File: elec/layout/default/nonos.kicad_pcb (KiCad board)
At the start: 2 copper layers, 45 x 122 mm, 74 parts, among them CN1 HRSHirose_DF40C_100DS_0_4V51, CN2 HRSHirose_DF40C_100DS_0_4V51, Q1 MOSFET, U1 STUSB4500QTR, U2 _Texas_Instruments_SN74LVC1G0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, U3 _Texas_Instruments_TAS5825MRH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, U5 JST_Sales_America_B02B_XASK_1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, U6 JST_Sales_America_B02B_XASK_1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, U7 _Texas_Instruments_TPS56637RP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

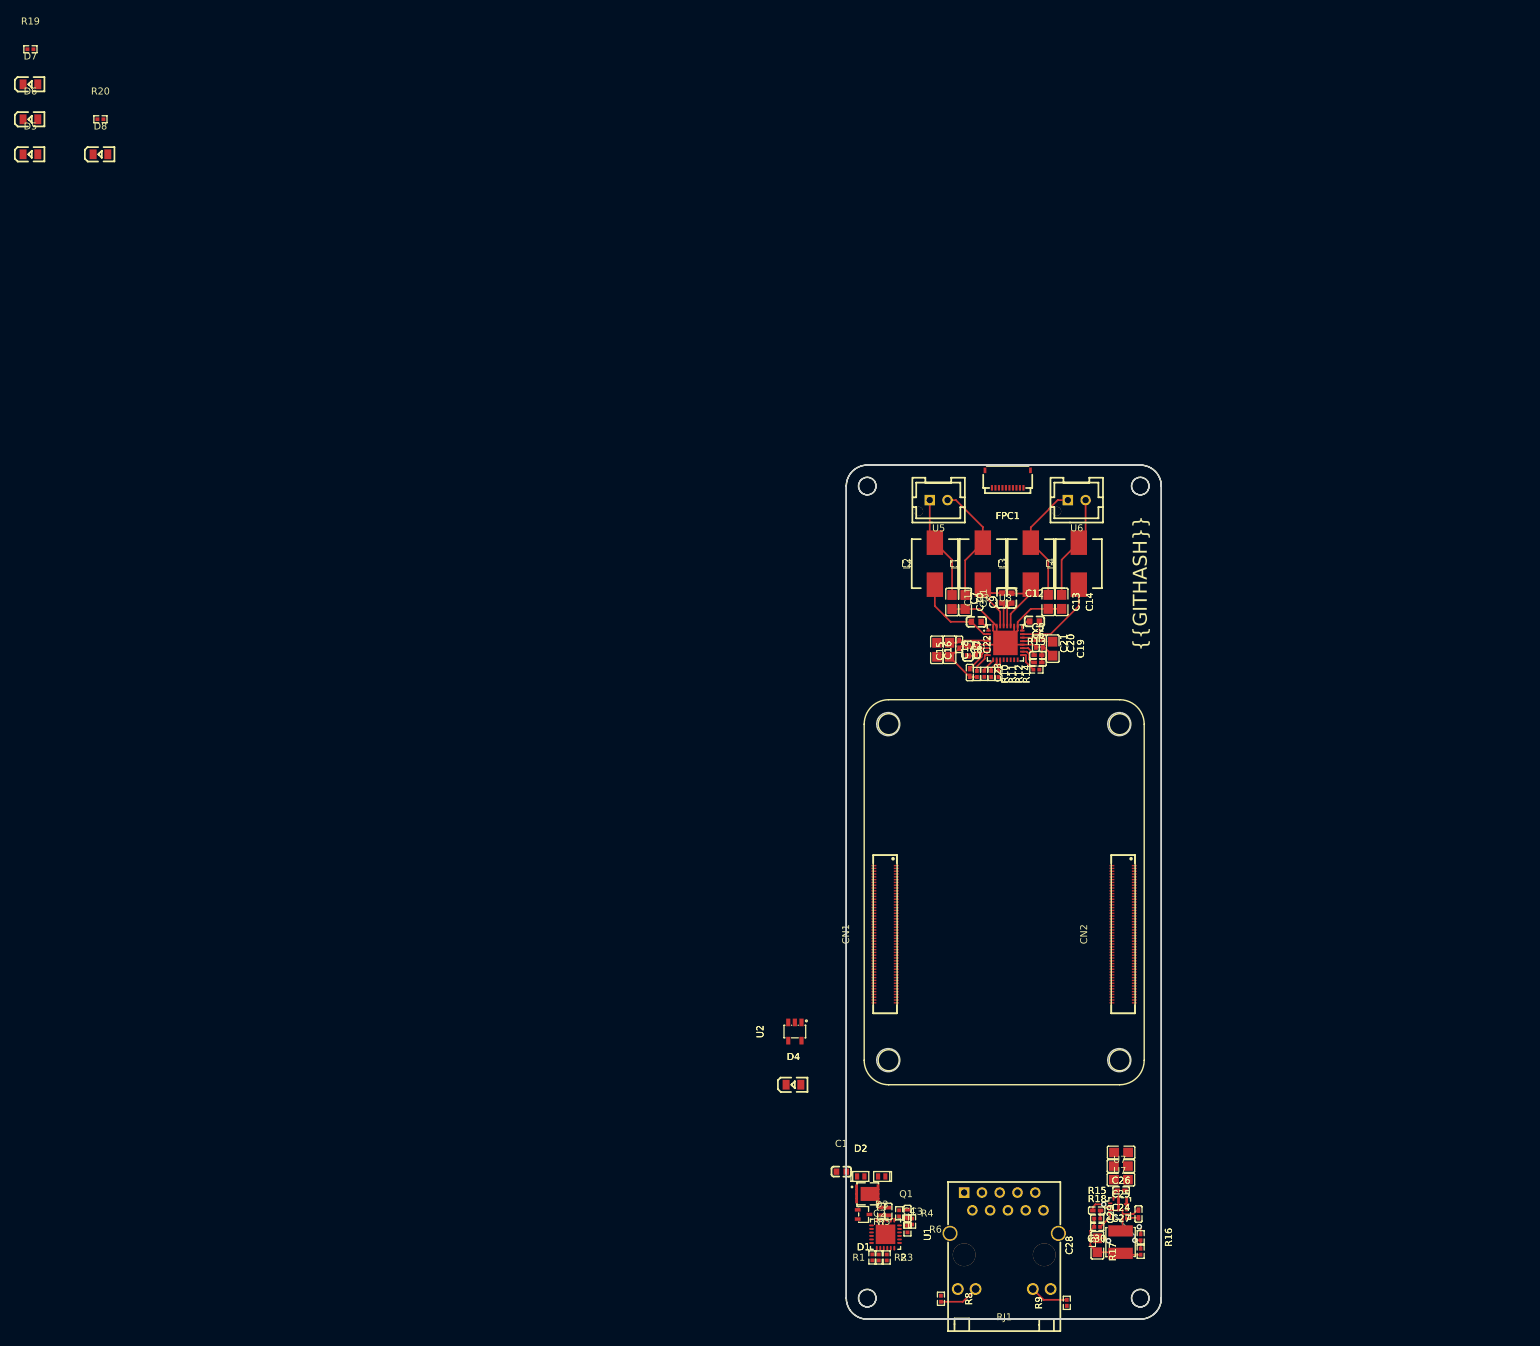
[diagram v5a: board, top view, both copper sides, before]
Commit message: refactor PD controller + remove params
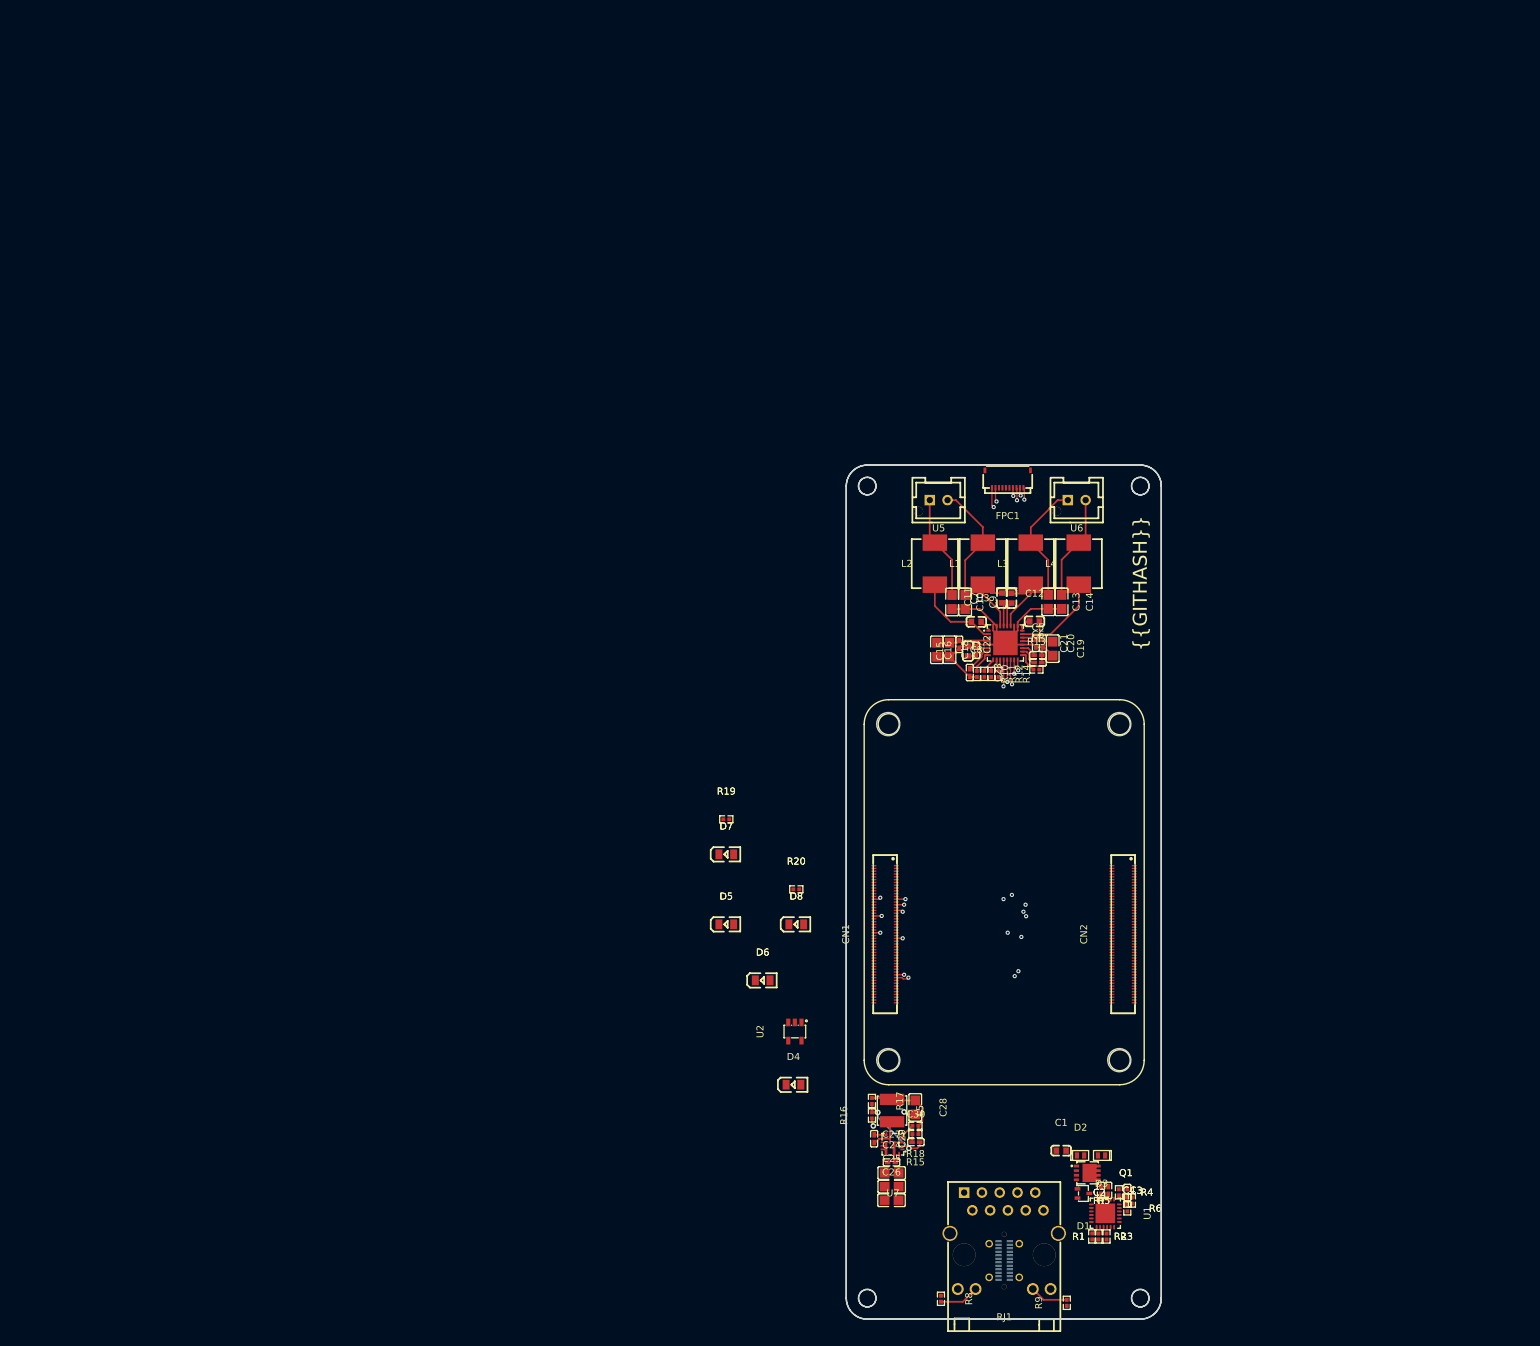
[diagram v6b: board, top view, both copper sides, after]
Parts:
- added U4: _HCTL_HC_TYPE_C_24P_VS9_3_5A_F1_1_04, lcsc:USB-C-SMD_HC-TYPE-C-24P-VS9.3-5A-F1.1-04, B.Cu at (139.1, 158.0)
- moved D6 161.5 mm to (104.6, 118.0)
- moved D5 148.3 mm to (99.4, 110.0)
- moved D7 148.3 mm to (99.4, 100.0)
- moved D8 148.3 mm to (109.4, 110.0)
- moved R19 148.3 mm to (99.4, 95.0)
- moved R20 148.3 mm to (109.4, 105.0)
- moved R17 44.0 mm to (120.2, 135.2), turned to -90 degrees
- moved R16 42.1 mm to (120.2, 137.3), turned to 90 degrees
- moved C29 39.3 mm to (120.5, 140.6), turned to -90 degrees
- moved L5 37.7 mm to (123.1, 136.6), turned to -90 degrees
- moved U7 33.7 mm to (123.2, 141.4), turned to 180 degrees
- moved C26 33.5 mm to (123.0, 149.4), turned to 0 degrees
- moved C27 33.0 mm to (123.0, 144.0), turned to 0 degrees
- moved C25 32.9 mm to (123.0, 147.5), turned to 0 degrees
- moved C24 32.8 mm to (123.0, 145.5), turned to 0 degrees
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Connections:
- net cathode renamed processor.power_3v3_led-cathode
- net cathode-1 renamed processor.power_5v_led-cathode
- net cathode-2 renamed processor.power_1v8_led-cathode
- C1 pad 1: lv -> GND
- C10 pad 2: lv -> GND
- C11 pad 1: amplifier-net-11 -> amplifier-net-5
- C11 pad 2: amplifier-net-2 -> amplifier-net-4
- C12 pad 1: amplifier-net-5 -> amplifier-net-3
- C12 pad 2: amplifier-net-6 -> amplifier-net-1
- C13 pad 1: net-4 -> net-3
- C13 pad 2: lv -> GND
- C14 pad 2: lv -> GND
- C15 pad 2: lv -> GND
- C16 pad 2: lv -> GND
- C17 pad 2: lv -> GND
- C18 pad 2: lv -> GND
- C19 pad 2: lv -> GND
- C2 pad 1: pd_controller-net-1 -> pd_controller-net-4
- C20 pad 2: lv -> GND
- C21 pad 2: lv -> GND
- C22 pad 2: lv -> GND
- C23 pad 1: amplifier-net-4 -> amplifier-net-7
- C23 pad 2: lv -> GND
- C24 pad 2: lv -> GND
- C25 pad 2: lv -> GND
- C26 pad 2: lv -> GND
- C27 pad 2: lv -> GND
- C28 pad 1: net-3 -> VCC_5V
- C28 pad 2: lv -> GND
- C29 pad 1: regulator-net-3 -> regulator-net-4
- C29 pad 2: regulator-net-2 -> regulator-net-3
- C3 pad 1: lv -> GND
- C4 pad 1: lv -> GND
- C5 pad 1: amplifier-net-8 -> amplifier-net-10
- C5 pad 2: lv -> GND
- C6 pad 1: amplifier-net-7 -> amplifier-net
- C6 pad 2: lv -> GND
- C7 pad 1: amplifier-net-10 -> amplifier-net-6
- C8 pad 1: amplifier-net-1 -> amplifier-net-2
- C8 pad 2: amplifier-net -> amplifier-net-8
- C9 pad 2: lv -> GND
- CN1 pad 10: pins[19] -> processor-net-3
- CN1 pad 14: processor-signal-7 -> processor-signal-3
- CN1 pad 15: signal-1 -> signal-7
- CN1 pad 17: signal-2 -> signal-5
- CN1 pad 23: processor-signal-2 -> processor-signal-6
- CN1 pad 24: processor-signal-5 -> processor-signal-7
- CN1 pad 28: signal -> signal-3
- CN1 pad 29: signal-7 -> signal-2
- CN1 pad 73: processor-signal-3 -> processor-signal-5
- CN1 pad 75: processor-signal-4 -> processor-signal-2
- CN1 pad 77: processor-signal-6 -> processor-signal-1
- CN1 pad 78: processor-pins[44] -> processor-pins[44]-1
- CN1 pad 81: processor-signal-1 -> processor-signal-9
- CN1 pad 82: signal-3 -> signal-6
- CN1 pad 85: processor-signal-9 -> processor-signal-4
- CN2 pad 78: processor-pins[44]-1 -> processor-pins[44]
- D1 pad 3: lv -> GND
- D2 pad 2: lv -> GND
- D3 pad 2: lv -> GND
- D4 pad 1: processor-net-2 -> VCC_3V3
- D5 pad 1: VCC_1V8 -> processor.power_1v8_led-anode
- D6 pad 1: VCC_3V3 -> processor.power_3v3_led-anode
- D7 pad 1: VCC_5V -> processor.power_5v_led-anode
- D8 pad 2: processor-net-1 -> processor-net-2
- FPC1 pad 10: signal-3 -> signal-6
- FPC1 pad 3: lv -> GND
- FPC1 pad 4: net-3 -> VCC_5V
- FPC1 pad 6: lv -> GND
- FPC1 pad 8: signal-2 -> signal-5
- FPC1 pad 9: signal-1 -> signal-7
- L2 pad 1: amplifier-net -> amplifier-net-8
- L3 pad 1: amplifier-net-2 -> amplifier-net-4
- L3 pad 2: net-4 -> net-3
- L4 pad 1: amplifier-net-6 -> amplifier-net-1
- L5 pad 1: net-3 -> VCC_5V
- L5 pad 2: regulator-net-2 -> regulator-net-3
- R10 pad 1: amplifier-net-3 -> amplifier-net-11
- R10 pad 2: lv -> GND
- R11 pad 1: signal-7 -> signal-2
- R12 pad 1: signal-5 -> signal
- R13 pad 1: signal -> signal-3
- R14 pad 1: signal-6 -> signal-1
- R15 pad 1: net-3 -> VCC_5V
- R16 pad 1: lv -> GND
- R17 pad 1: net-3 -> VCC_5V
- R18 pad 1: net-3 -> VCC_5V
- R18 pad 2: regulator-net-4 -> regulator-net-2
- R19 pad 2: VCC_3V3 -> processor-net-1
- R20 pad 1: processor-net-1 -> processor-net-2
- R20 pad 2: GND -> processor-net-3
- R6 pad 2: pd_controller-net-4 -> pd_controller-net-1
- R7 pad 2: pd_controller-net-1 -> pd_controller-net-4
- R8 pad 2: rj45-net -> rj45-net-1
- R9 pad 2: rj45-net-1 -> rj45-net
- RJ1 pad 12: rj45-net -> rj45-net-1
- RJ1 pad 13: rj45-net-1 -> rj45-net
- RJ1 pad SHIELD0: lv -> GND
- RJ1 pad SHIELD1: lv -> GND
- U1 pad 10: lv -> GND
- U1 pad 12: lv -> GND
- U1 pad 13: lv -> GND
- U1 pad 16: pd_controller-net-4 -> pd_controller-net-1
- U1 pad 22: lv -> GND
- U1 pad 25: lv -> GND
- U1 pad 6: lv -> GND
- U2 pad 4: processor-net-2 -> processor-net-1
- U3 pad 1: amplifier-net-1 -> amplifier-net-2
- U3 pad 10: signal-5 -> signal
- U3 pad 11: signal-6 -> signal-1
- U3 pad 17: signal -> signal-3
- U3 pad 18: amplifier-net-7 -> amplifier-net
- U3 pad 19: amplifier-net-8 -> amplifier-net-10
- U3 pad 2: amplifier-net -> amplifier-net-8
- U3 pad 20: lv -> GND
- U3 pad 23: amplifier-net-6 -> amplifier-net-1
- U3 pad 24: amplifier-net-5 -> amplifier-net-3
- U3 pad 25: lv -> GND
- U3 pad 26: lv -> GND
- U3 pad 27: amplifier-net-2 -> amplifier-net-4
- U3 pad 28: amplifier-net-11 -> amplifier-net-5
- U3 pad 29: amplifier-net-10 -> amplifier-net-6
- U3 pad 31: lv -> GND
- U3 pad 32: lv -> GND
- U3 pad 33: lv -> GND
- U3 pad 5: lv -> GND
- U3 pad 7: amplifier-net-4 -> amplifier-net-7
- U3 pad 8: amplifier-net-3 -> amplifier-net-11
- U3 pad 9: signal-7 -> signal-2
- U6 pad 1: net-4 -> net-3
- U7 pad 10: lv -> GND
- U7 pad 3: lv -> GND
- U7 pad 4: regulator-net-4 -> regulator-net-2
- U7 pad 6: regulator-net-2 -> regulator-net-3
- U7 pad 7: regulator-net-3 -> regulator-net-4
- U7 pad 9: lv -> GND
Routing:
- net SDA: track 0.00 -> 91.0 mm, vias 0 -> 4
- net SCL: track 0.00 -> 90.2 mm, vias 0 -> 4
- net signal-4: track 0.00 -> 84.9 mm, vias 0 -> 3
- net signal-6: track 3.34 -> 87.3 mm, vias 0 -> 3
- net signal-5: track 1.70 -> 82.1 mm, vias 0 -> 3
- net signal-7: track 2.11 -> 81.6 mm, vias 0 -> 3
- net GND: track 0.00 -> 59.2 mm, vias 0 -> 2
- net lv: track 59.2 -> 0.00 mm, vias 2 -> 0
- net I2S_SCK: track 0.00 -> 58.1 mm, vias 0 -> 3
- net I2S_SD: track 0.00 -> 54.0 mm, vias 0 -> 3
- net I2S_WS: track 0.00 -> 49.8 mm, vias 0 -> 3
- net net-4: track 17.4 -> 0.00 mm
- net VCC_5V: track 0.00 -> 11.8 mm
- net amplifier-net-5: track 14.6 -> 3.53 mm
- net regulator-net: track 1.80 -> 12.3 mm, vias 0 -> 2
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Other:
- copper layers 2 -> 4

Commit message: layout 95%
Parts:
- removed D6, D7, D8: , lcsc:LED0805-R-RD
- added HDR1: HCTL_PZ254_2_04_S, lcsc:HDR-SMD_8P-P2.54-V-M-R2-C4-LS7.4, F.Cu at (169.4, 130.9)
- added HDR2: HCTL_PZ254_2_04_S, lcsc:HDR-SMD_8P-P2.54-V-M-R2-C4-LS7.4, F.Cu at (169.4, 62.9)
- C2: value 100nF ±10% 16V X7R -> 1µF ±10% 25V X5R
- C4: value 1µF ±10% 25V X5R -> 100nF ±10% 16V X7R
- moved D4 76.2 mm to (134.6, 61.1), turned to 90 degrees
- moved U2 63.2 mm to (133.0, 66.7), turned to -90 degrees
- moved D5 59.1 mm to (132.6, 61.1), turned to 90 degrees
- moved R20 47.3 mm to (133.3, 64.1)
- moved R19 46.9 mm to (135.0, 64.5), turned to -90 degrees
- moved R3 22.5 mm to (137.3, 138.0), turned to 90 degrees
- moved R1 21.6 mm to (137.7, 140.1), turned to 0 degrees
- moved R2 21.3 mm to (138.3, 138.0), turned to 90 degrees
- moved R6 21.1 mm to (137.3, 142.3), turned to 0 degrees
- moved R5 21.0 mm to (137.3, 143.3), turned to 180 degrees
- moved R7 18.6 mm to (139.1, 143.5), turned to 0 degrees
- moved D3 17.8 mm to (135.2, 143.0), turned to 0 degrees
- moved U4 16.8 mm to (153.2, 149.0)
- moved C23 16.6 mm to (148.4, 65.4)
- moved R11 16.6 mm to (150.5, 65.6)
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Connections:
- net pd_controller.PD_CONTROLLER-signal renamed pd_controller.pd_controller-signal-1
- net pd_controller.PD_CONTROLLER-signal-1 renamed pd_controller.pd_controller-signal
- net pd_controller.PD_CONTROLLER.footprint.pins[18].net-net renamed pd_controller.pd_controller.footprint.pins[18].net-net
- net pins[40] renamed processor.hdi_b-pins[40]
- net pins[46] renamed processor-pins[46]-1
- net pins[49] renamed processor.hdi_b-pins[49]
- net processor-signal-8 renamed processor-pins[49]
- net processor.hdi_b-pins[23] renamed pins[23]
- net processor.hdi_b-pins[26] renamed pins[26]
- net processor.hdi_b-pins[28] renamed pins[28]
- C10 pad 1: net -> net-2
- C11 pad 1: amplifier-net-5 -> amplifier-net-3
- C11 pad 2: amplifier-net-4 -> amplifier-net-2
- C12 pad 1: amplifier-net-3 -> amplifier-net-7
- C12 pad 2: amplifier-net-1 -> amplifier-net
- C13 pad 1: net-3 -> net-1
- C14 pad 1: net-1 -> net
- C2 pad 1: pd_controller-net-4 -> GND
- C2 pad 2: VBUS -> VREG_1V2
- C23 pad 1: amplifier-net-7 -> amplifier-net-6
- C29 pad 1: regulator-net-4 -> regulator-net
- C29 pad 2: regulator-net-3 -> regulator-net-1
- C3 pad 2: VREG_1V2 -> VREG_2V7
- C30 pad 1: regulator-net-1 -> regulator-net-2
- C30 pad 2: regulator-net -> regulator-net-3
- C4 pad 1: GND -> pd_controller-net-3
- C4 pad 2: VREG_2V7 -> VBUS
- C6 pad 1: amplifier-net -> amplifier-net-1
- C7 pad 1: amplifier-net-6 -> amplifier-net-11
- C7 pad 2: amplifier-net-9 -> amplifier-net-8
- C8 pad 1: amplifier-net-2 -> amplifier-net-4
- C8 pad 2: amplifier-net-8 -> amplifier-net-5
- C9 pad 1: net-2 -> net-3
- CN1 pad 10: processor-net-3 -> processor-net-2
- CN1 pad 12: processor-pins[23] -> processor-signal
- CN1 pad 14: processor-signal-3 -> UART_TX
- CN1 pad 15: signal-7 -> signal-3
- CN1 pad 17: signal-5 -> signal-4
- CN1 pad 22: pins[43] -> processor-signal-3
- CN1 pad 23: processor-signal-6 -> pins[45]
- CN1 pad 24: processor-signal-7 -> processor-signal-2
- CN1 pad 27: signal-4 -> signal-5
- CN1 pad 28: signal-3 -> signal-2
- CN1 pad 29: signal-2 -> signal-1
- CN1 pad 73: processor-signal-5 -> UART_RX
- CN1 pad 75: processor-signal-2 -> pins[50]
- CN1 pad 77: processor-signal-1 -> processor-pins[46]
- CN1 pad 78: processor-pins[44]-1 -> processor-pins[44]
- CN1 pad 80: processor-signal -> processor-pins[40]
- CN1 pad 81: processor-signal-9 -> processor-signal-1
- CN1 pad 82: signal-6 -> signal
- CN1 pad 85: processor-signal-4 -> processor-signal-6
- CN1 pad 86: processor-pins[28] -> processor-signal-5
- CN1 pad 87: processor-pins[26] -> processor-signal-4
- CN2 pad 78: processor-pins[44] -> processor-pins[44]-1
- D4 pad 2: processor-net -> processor-net-3
- D5 pad 1: processor.power_1v8_led-anode -> VCC_3V3
- D5 pad 2: processor.power_1v8_led-cathode -> processor-net-1
- FPC1 pad 10: signal-6 -> signal
- FPC1 pad 7: signal-4 -> signal-5
- FPC1 pad 8: signal-5 -> signal-4
- FPC1 pad 9: signal-7 -> signal-3
- L1 pad 1: amplifier-net-9 -> amplifier-net-8
- L1 pad 2: net-2 -> net-3
- L2 pad 1: amplifier-net-8 -> amplifier-net-5
- L2 pad 2: net -> net-2
- L3 pad 1: amplifier-net-4 -> amplifier-net-2
- L3 pad 2: net-3 -> net-1
- L4 pad 1: amplifier-net-1 -> amplifier-net
- L4 pad 2: net-1 -> net
- L5 pad 2: regulator-net-3 -> regulator-net-1
- Q1 pad 1: pd_controller.VSINK_MOSFET.footprint.pins[0].net-net -> VBUS
- Q1 pad 2: pd_controller.VSINK_MOSFET.footprint.pins[1].net-net -> VBUS
- Q1 pad 4: pd_controller-net -> pd_controller-net-2
- Q1 pad 5: pd_controller.VSINK_MOSFET.footprint.pins[4].net-net -> VSINK_VCC
- Q1 pad 6: pd_controller.VSINK_MOSFET.footprint.pins[5].net-net -> VSINK_VCC
- Q1 pad 7: pd_controller.VSINK_MOSFET.footprint.pins[6].net-net -> VSINK_VCC
- Q1 pad 8: pd_controller.VSINK_MOSFET.footprint.pins[7].net-net -> VSINK_VCC
- R1 pad 2: pd_controller-net-3 -> pd_controller-net-1
- R10 pad 1: amplifier-net-11 -> amplifier-net-9
- R11 pad 1: signal-2 -> signal-1
- R12 pad 1: signal -> signal-7
- R13 pad 1: signal-3 -> signal-2
- R14 pad 1: signal-1 -> signal-6
- R15 pad 2: regulator-net-1 -> regulator-net-2
- R16 pad 2: regulator-net -> regulator-net-3
- R17 pad 2: regulator-net -> regulator-net-3
- R18 pad 2: regulator-net-2 -> regulator-net-4
- R19 pad 1: processor-net -> processor-net-3
- R19 pad 2: processor-net-1 -> processor-net-2
- R2 pad 1: I2C_SCL -> SCL
- R2 pad 2: hv -> VCC_3V3
- R20 pad 1: processor-net-2 -> processor-net-1
- R20 pad 2: processor-net-3 -> processor-net
- R3 pad 1: I2C_SDA -> SDA
- R3 pad 2: hv -> VCC_3V3
- R4 pad 2: pd_controller-net-2 -> pd_controller-net
- R5 pad 1: pd_controller-net -> pd_controller-net-2
- R6 pad 1: pd_controller-net -> pd_controller-net-2
- R6 pad 2: pd_controller-net-1 -> pd_controller-net-4
- R7 pad 1: pd_controller-net -> pd_controller-net-2
- R7 pad 2: pd_controller-net-4 -> pd_controller-net-3
- U1 pad 16: pd_controller-net-1 -> pd_controller-net-4
- U1 pad 18: pd_controller-net-2 -> pd_controller-net
- U1 pad 7: I2C_SCL -> SCL
- U1 pad 8: I2C_SDA -> SDA
- U1 pad 9: pd_controller-net-3 -> pd_controller-net-1
- U2 pad 4: processor-net-1 -> processor-net
- U3 pad 1: amplifier-net-2 -> amplifier-net-4
- U3 pad 10: signal -> signal-7
- U3 pad 11: signal-1 -> signal-6
- U3 pad 17: signal-3 -> signal-2
- U3 pad 18: amplifier-net -> amplifier-net-1
- U3 pad 2: amplifier-net-8 -> amplifier-net-5
- U3 pad 23: amplifier-net-1 -> amplifier-net
- U3 pad 24: amplifier-net-3 -> amplifier-net-7
- U3 pad 27: amplifier-net-4 -> amplifier-net-2
- U3 pad 28: amplifier-net-5 -> amplifier-net-3
- U3 pad 29: amplifier-net-6 -> amplifier-net-11
- U3 pad 30: amplifier-net-9 -> amplifier-net-8
- U3 pad 7: amplifier-net-7 -> amplifier-net-6
- U3 pad 8: amplifier-net-11 -> amplifier-net-9
- U3 pad 9: signal-2 -> signal-1
- U4 pad 25: usb_connector.connector-net -> GND
- U4 pad 26: usb_connector.connector-net -> GND
- U4 pad 27: usb_connector.connector-net -> GND
- U4 pad 28: usb_connector.connector-net -> GND
- U4 pad A1: usb_connector.connector-net-1 -> GND
- U4 pad A12: usb_connector.connector-net-1 -> GND
- U4 pad A4: VSINK_VCC -> VBUS
- U4 pad A6: usb_connector-net-1 -> usb_connector-net
- U4 pad A7: usb_connector-net -> usb_connector-net-1
- U4 pad A9: VSINK_VCC -> VBUS
- U4 pad B1: usb_connector.connector-net-1 -> GND
- U4 pad B12: usb_connector.connector-net-1 -> GND
- U4 pad B4: VSINK_VCC -> VBUS
- U4 pad B5: CC1 -> CC2
- U4 pad B6: usb_connector-net-1 -> usb_connector-net
- U4 pad B7: usb_connector-net -> usb_connector-net-1
- U4 pad B9: VSINK_VCC -> VBUS
- U5 pad 1: net -> net-2
- U5 pad 2: net-2 -> net-3
- U6 pad 1: net-3 -> net-1
- U6 pad 2: net-1 -> net
- U7 pad 2: regulator-net -> regulator-net-3
- U7 pad 4: regulator-net-2 -> regulator-net-4
- U7 pad 6: regulator-net-3 -> regulator-net-1
- U7 pad 7: regulator-net-4 -> regulator-net
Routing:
- net VCC_5V: track 11.8 -> 136.2 mm, vias 0 -> 4
- net signal-6: track 87.3 -> 1.70 mm, vias 3 -> 0
- net signal: track 1.91 -> 87.2 mm, vias 0 -> 3
- net signal-7: track 81.6 -> 1.91 mm, vias 3 -> 0
- net signal-3: track 3.34 -> 82.1 mm, vias 0 -> 3
- net ETH_LED_ACTIVITY: track 0.00 -> 78.5 mm, vias 0 -> 2
- net ETH_LED_LINK: track 0.00 -> 70.0 mm, vias 0 -> 2
- net ETH_P3_N: track 0.00 -> 69.5 mm, vias 0 -> 2
- net ETH_P3_P: track 0.00 -> 68.8 mm, vias 0 -> 2
- net ETH_P1_P: track 0.00 -> 67.0 mm, vias 0 -> 1
- net SDA: track 91.0 -> 157.3 mm, vias 4 -> 6
- net SCL: track 90.2 -> 154.3 mm, vias 4 -> 6
- net ETH_P2_N: track 0.00 -> 63.5 mm, vias 0 -> 2
- net ETH_P2_P: track 0.00 -> 60.3 mm, vias 0 -> 2
- net ETH_P1_N: track 0.00 -> 58.1 mm, vias 0 -> 1
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- added copper zone on F.Cu, net GND
- added copper zone on In2.Cu, net GND
- added copper zone on F.Cu, net VBUS
- added copper zone on F.Cu, net VCC_5V
- added copper zone on B.Cu, net VSINK_VCC
- added copper zone on F.Cu, net VSINK_VCC
- added copper zone on F.Cu, net amplifier-net
- added copper zone on F.Cu, net amplifier-net-2
- added copper zone on F.Cu, net amplifier-net-5
- added copper zone on F.Cu, net amplifier-net-8
- added copper zone on F.Cu, net net
- added copper zone on F.Cu, net net-1
- added copper zone on F.Cu, net net-2
- added copper zone on F.Cu, net net-3
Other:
- outline, holes or cut-outs redrawn
- board text added: "5V"
- board text added: "CM4 ACTVITY"
- board text added: "CM4 PWR"
- board text added: "NONOS"
- board text added: "RX"
- board text added: "SCK"
- board text added: "SCL"
- board text added: "SD"
- board text added: "SDA"
- board text added: "TX"
- board text added: "WS"

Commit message: layout complete
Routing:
- net signal-2: track 3.34 -> 56.3 mm, vias 0 -> 3
- net signal-1: track 2.11 -> 50.2 mm, vias 0 -> 3
- net VBUS: track 3.71 -> 22.1 mm, vias 4 -> 8
- net VCC_3V3: track 11.5 -> 22.8 mm, vias 6 -> 19
- net GND: track 68.5 -> 76.4 mm, vias 2 -> 45
- net usb_connector-net: track 0.00 -> 5.79 mm, vias 0 -> 2
- net usb_connector-net-1: track 0.00 -> 1.83 mm
- net VCC_5V: track 136.2 -> 136.7 mm
- added copper zone on B.Cu, net VCC_3V3
- added copper zone on In1.Cu, net VCC_3V3
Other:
- board text added: "TWEETER"
- board text added: "WOOFER"
